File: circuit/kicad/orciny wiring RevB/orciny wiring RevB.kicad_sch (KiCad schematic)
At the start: 0 parts

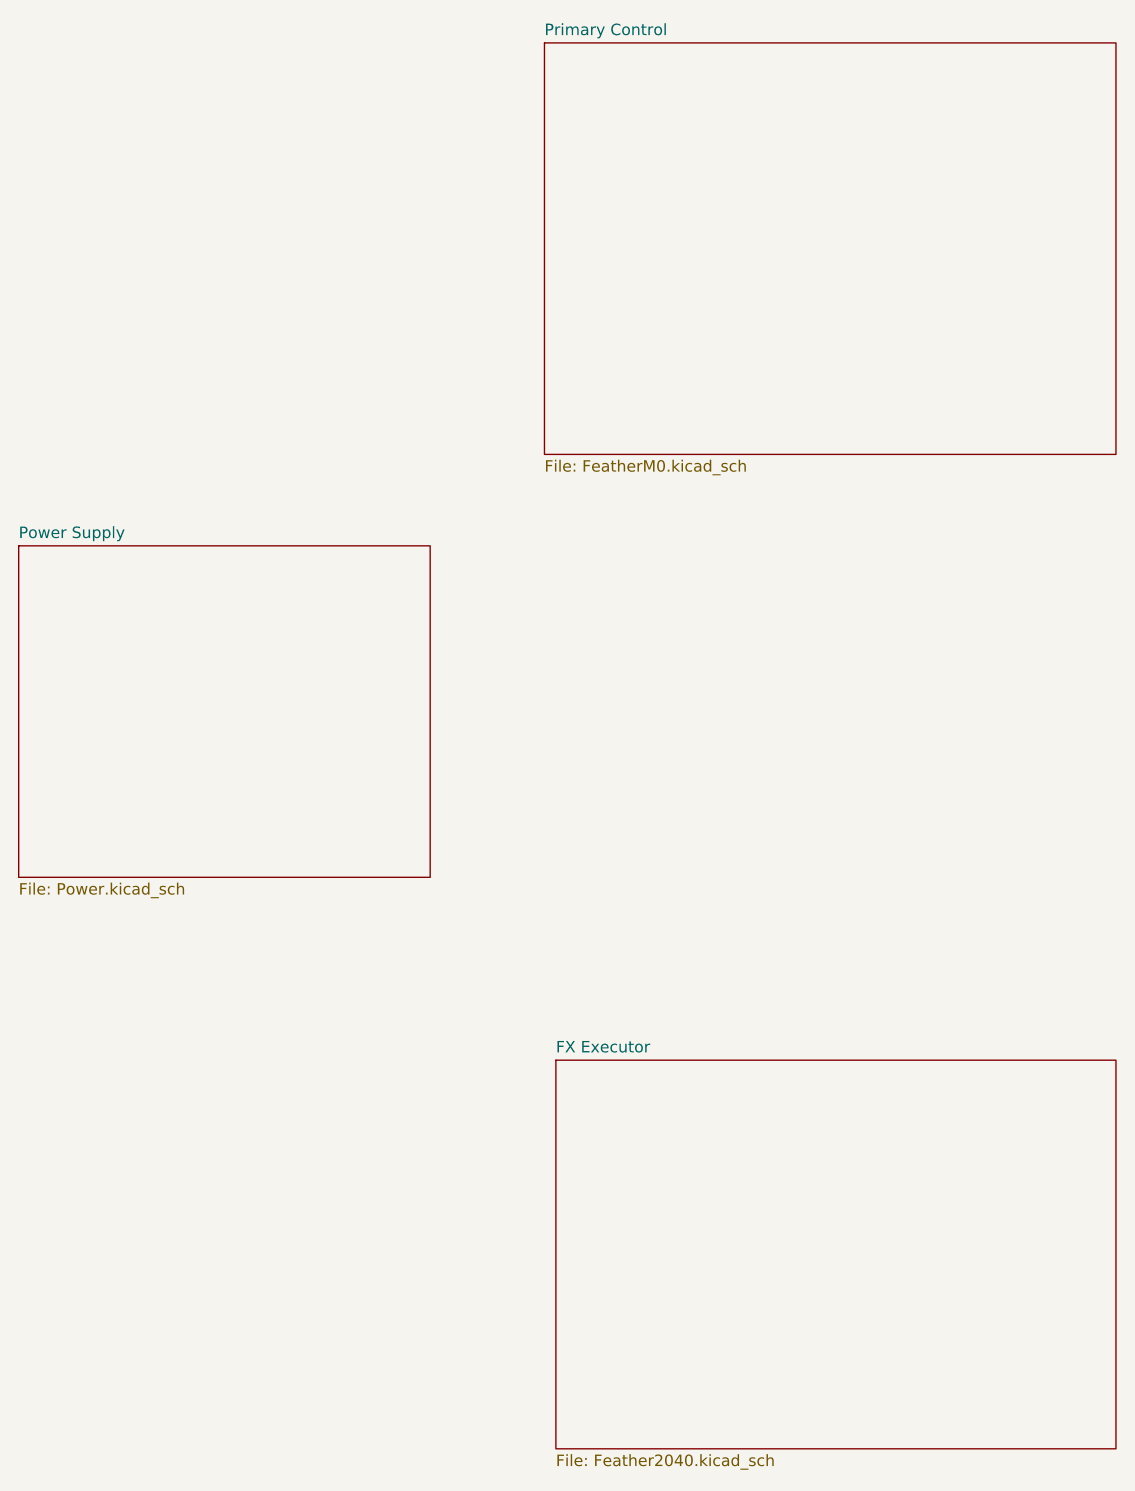
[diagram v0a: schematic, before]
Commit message: Full-sweep cleanup: align README, BOM, netmap, and KiCad hierarchy for RP2040-only design
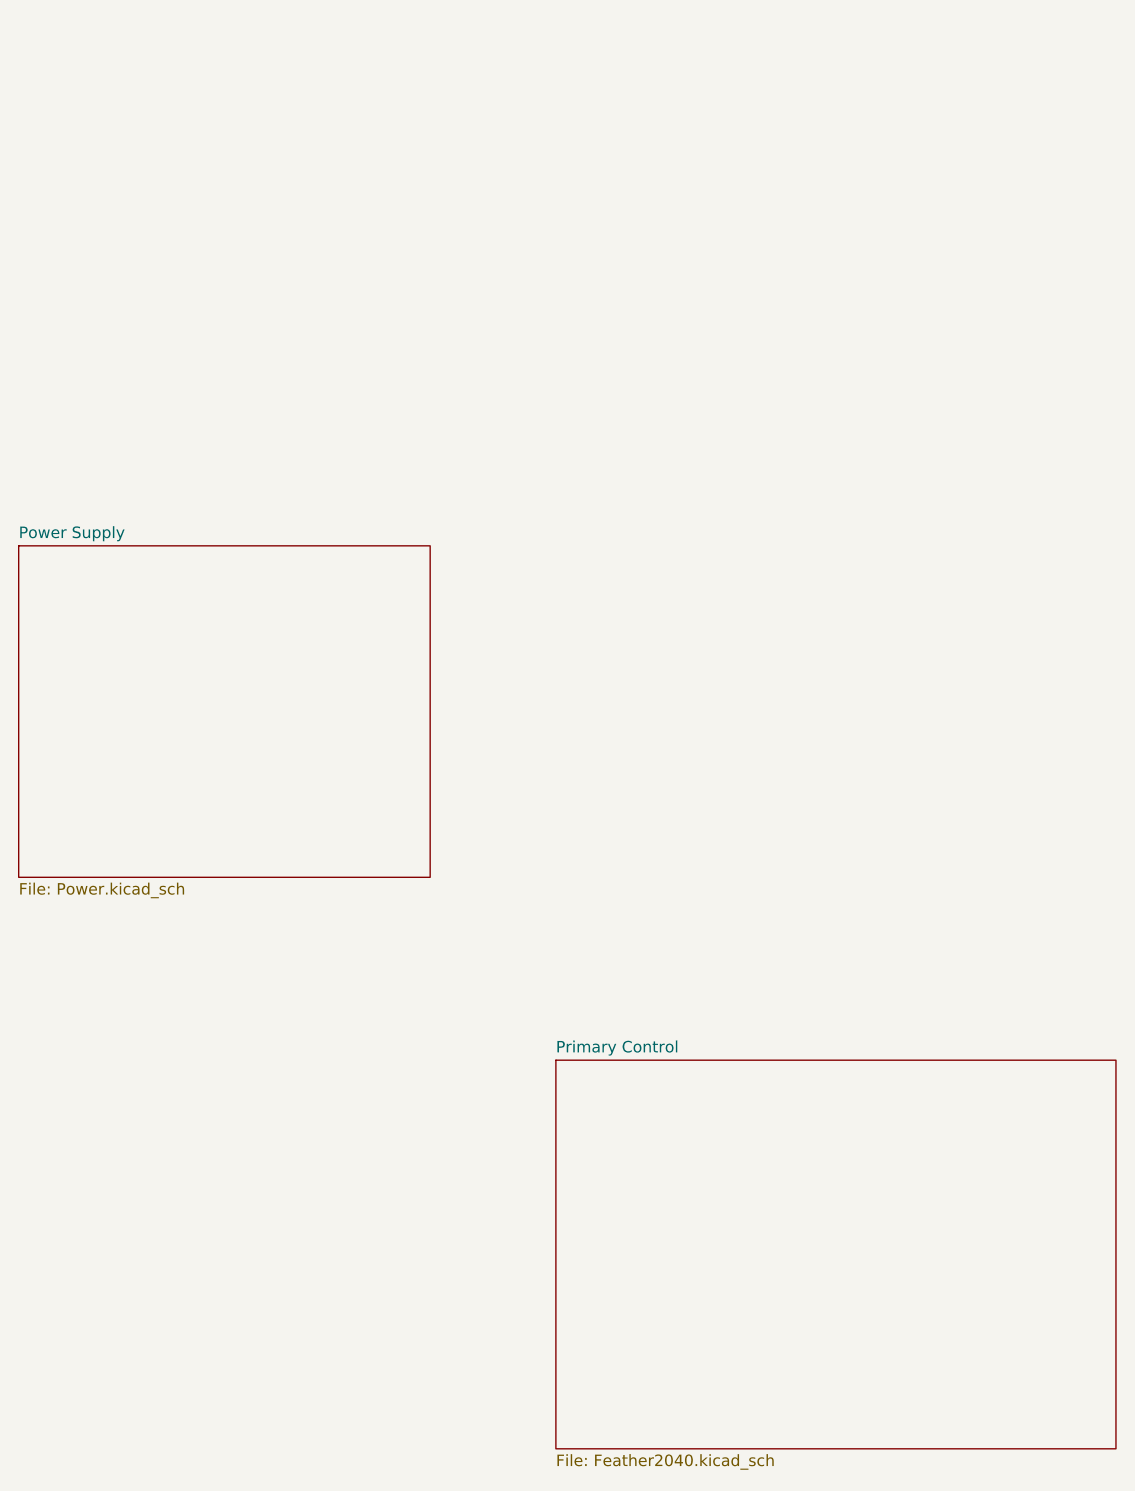
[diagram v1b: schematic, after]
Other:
- removed sheet FX Executor
- sheet Primary Control: file FeatherM0.kicad_sch -> Feather2040.kicad_sch
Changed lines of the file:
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@@
-	)
-	(sheet
-		(at 74.93 22.86)
-		(size 63.5 45.72)
-		(exclude_from_sim no)
-		(in_bom yes)
-		(on_board yes)
-		(dnp no)
-		(fields_autoplaced yes)
-		(stroke
-			(width 0.1524)
-			(type solid)
-		)
-		(fill
-			(color 0 0 0 0.0000)
-		)
-		(property "Sheetname" "Primary Control"
-			(at 74.93 22.1484 0)
-			(effects
-				(font
-					(size 1.27 1.27)
-				)
-				(justify left bottom)
-			)
-		)
-		(property "Sheetfile" "FeatherM0.kicad_sch"
-			(at 74.93 69.1646 0)
-			(effects
-				(font
-					(size 1.27 1.27)
-				)
-				(justify left top)
-			)
-		)
-		(instances
-			(project "orciny wiring RevB"
-				(path "/bfdec584-7582-4877-889f-0fbbd4c2f894"
-					(page "3")
-				)
-			)
-		)
 	)
 	(sheet
@@
 			(color 0 0 0 0.0000)
 		)
-		(property "Sheetname" "FX Executor"
+		(property "Sheetname" "Primary Control"
 			(at 76.2 135.1784 0)
 			(effects
